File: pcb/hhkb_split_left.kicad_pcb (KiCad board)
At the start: 2 copper layers, 140.4 x 97.4 mm, 74 parts, among them SW1 Esc, SW10 E, SW11 R, SW12 T, SW13 Ctrl, SW14 A, SW15 S, SW16 D, SW17 F, SW18 G, SW19 Shift, SW2 1, SW20 Z, SW21 X, SW22 C, SW23 V, SW24 B, SW25 Alt, SW26 Meta, SW27 L-Space, SW3 2, SW4 3, SW5 4, SW6 5, SW7 Tab, SW8 Q, SW9 W, U1 74LVC595

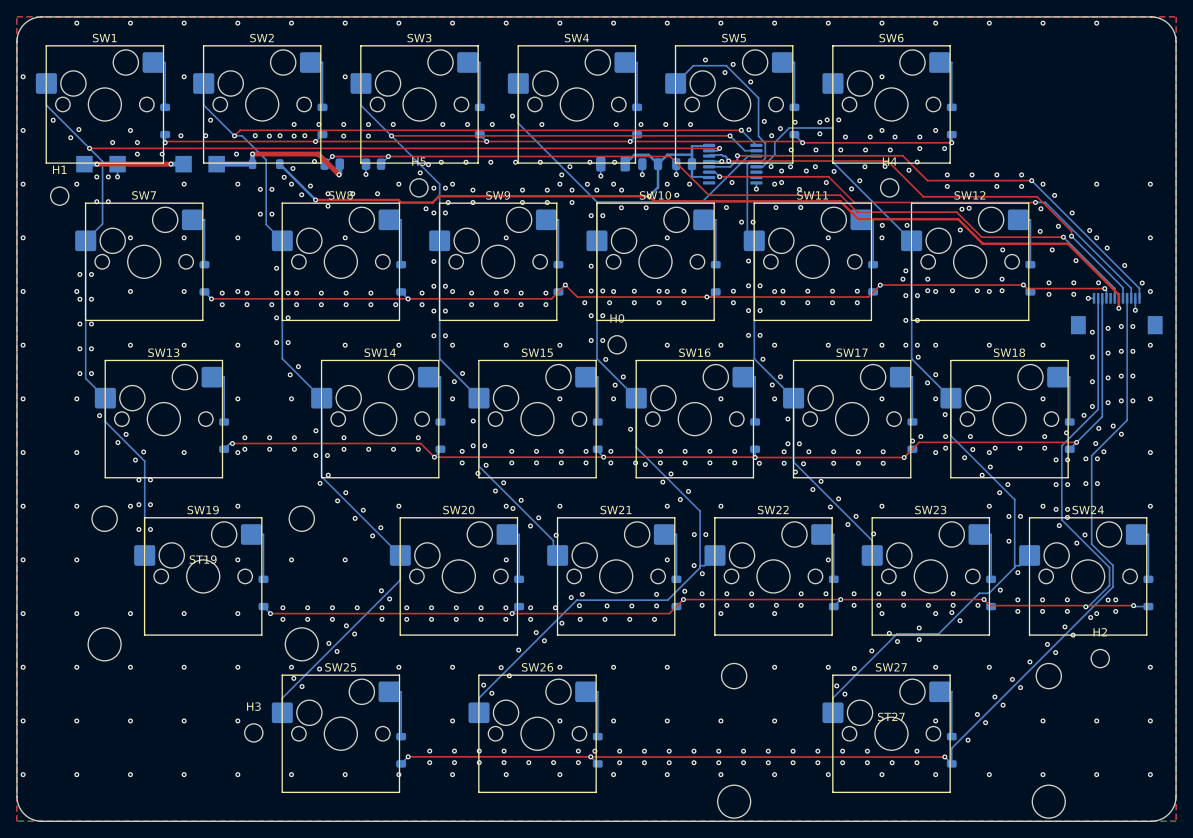
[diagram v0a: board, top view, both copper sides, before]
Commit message: DSNクリアランスマージンを左右共通15µmに確定（未配線 左0/右1）
利用者の要望「左右で違うマージン値を使う非対称は避けたい」に従い、
基板ごとに別マージンを使う案は取り下げ。**共通の値**で両基板の
未配線最小・DRC違反0を両立する値を総当たりで再探索した。

  M=15  左右とも DRC違反0。未配線は左右の Freerouting 実行タイミングで
        0〜2 の間で揺れる（同じ入力で 3 回実行して確認）。今回のコミット
        時点では 左0・右1（COL8-SW31、基板最遠端の列。過去の探索で
        構造的な残りと確認済み）

Freerouting 自身が打つビア（層間移動用）が規則ぎりぎりで他ネットに
近すぎることがあり、その 1 本を DRC の座標情報から直接押し出す
`gnd_fanout.nudge_tight_vias` を試作した。**失敗して撤回した。**
DRC の `pos` はアイテムの代表点であって実際の最近接距離ではないため、
「相手からの距離」を計算しても無関係な値になり、修正が一度も発火
しなかった（デバッグで dist=1.088mm という無意味な値を確認）。
この方式では直せない。実装は削除済み。

Co-Authored-By: Claude Sonnet 5 <noreply@anthropic.com>
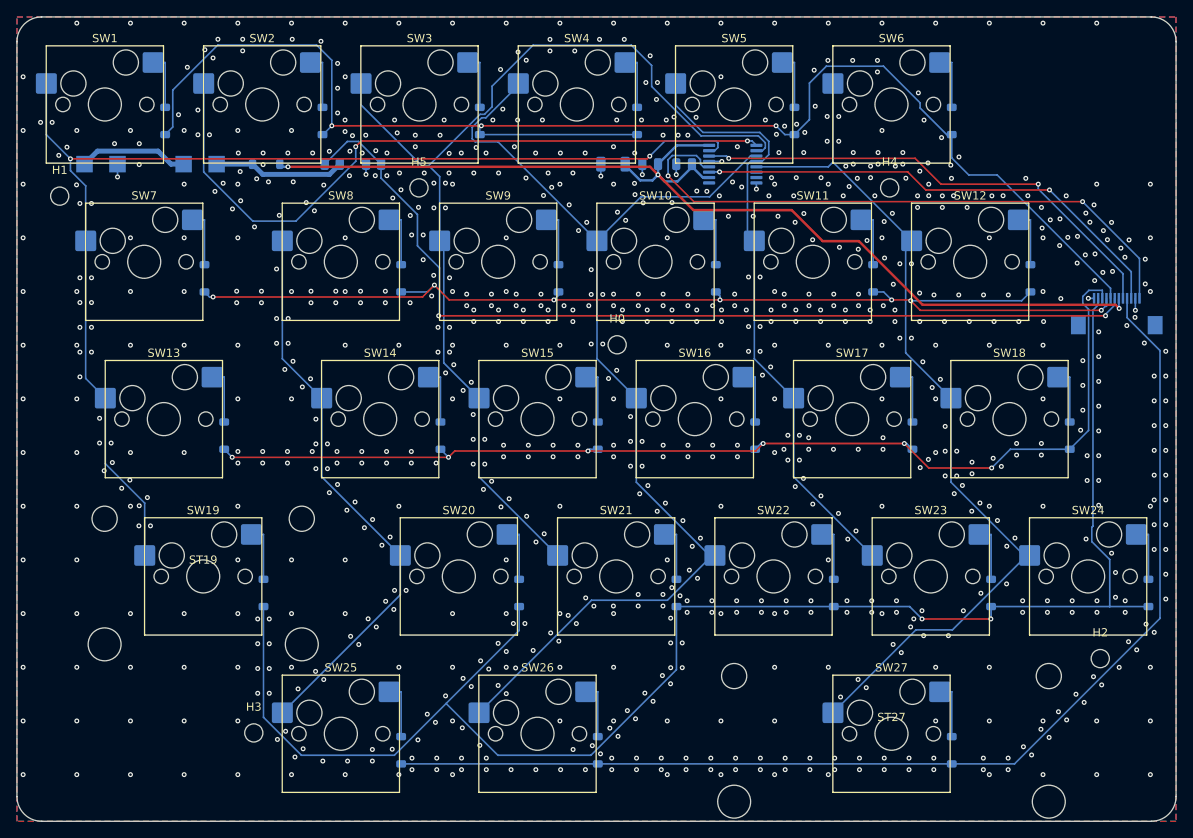
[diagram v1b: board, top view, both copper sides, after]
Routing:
- net ROW0: track 102.3 -> 172.9 mm, vias 6 -> 3
- net ROW3: track 156.4 -> 195.6 mm, vias 7 -> 2
- net ROW1: track 118.8 -> 136.8 mm
- net CS: track 60.8 -> 74.1 mm
- net COL2: track 111.9 -> 124.0 mm, vias 2 -> 0
- net VBATT_SENSE: track 105.2 -> 113.8 mm, vias 3 -> 2
- net COL3: track 126.8 -> 133.5 mm
- net ROW2: track 129.8 -> 134.2 mm
- net COL5: track 112.5 -> 108.7 mm
- net ROW4: track 135.9 -> 139.6 mm, vias 3 -> 0
- net VBATT_SW: track 18.4 -> 15.9 mm, vias 2 -> 0
- net COL4: track 76.3 -> 74.0 mm
- net COL0: track 141.5 -> 143.3 mm
- net V3V3: track 133.4 -> 132.0 mm
- net VBATT_RAW: track 12.0 -> 13.3 mm, vias 2 -> 0
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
